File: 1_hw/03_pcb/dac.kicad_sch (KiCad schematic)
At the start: 6 parts, among them U17 AD9850, U18 AD9744

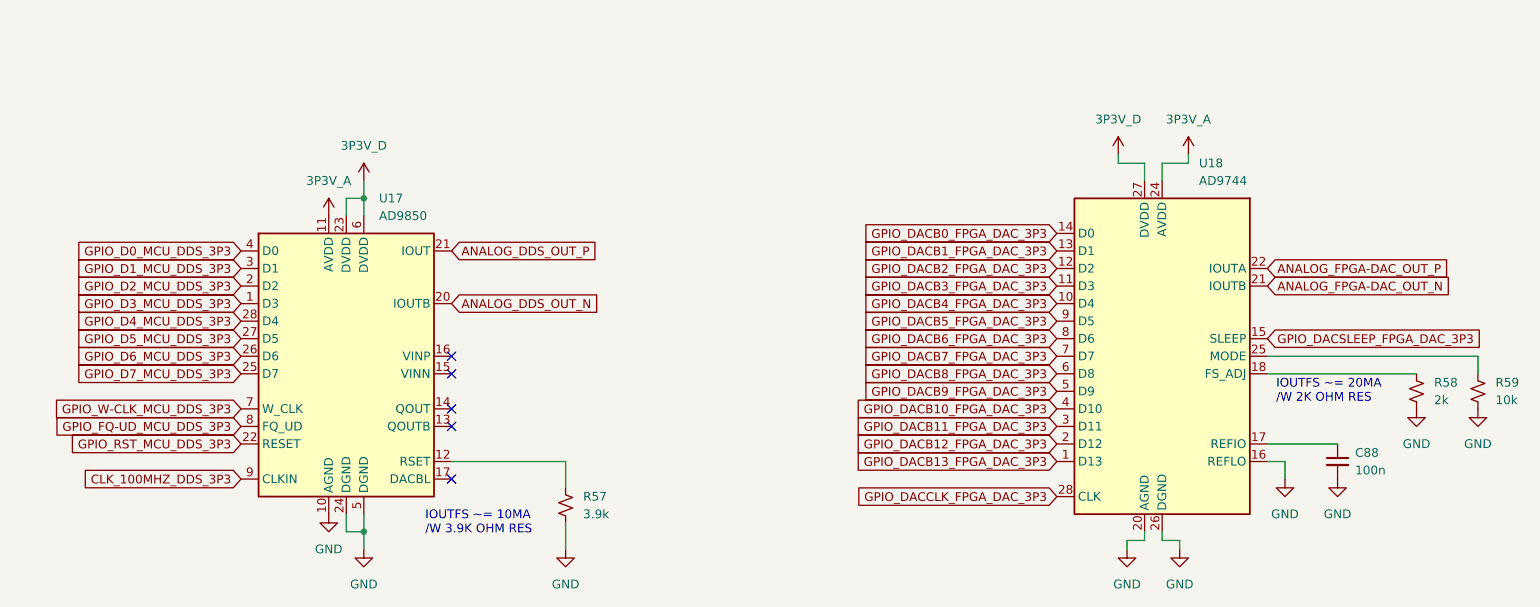
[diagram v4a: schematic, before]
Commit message: FEAT: Initial board placement started.
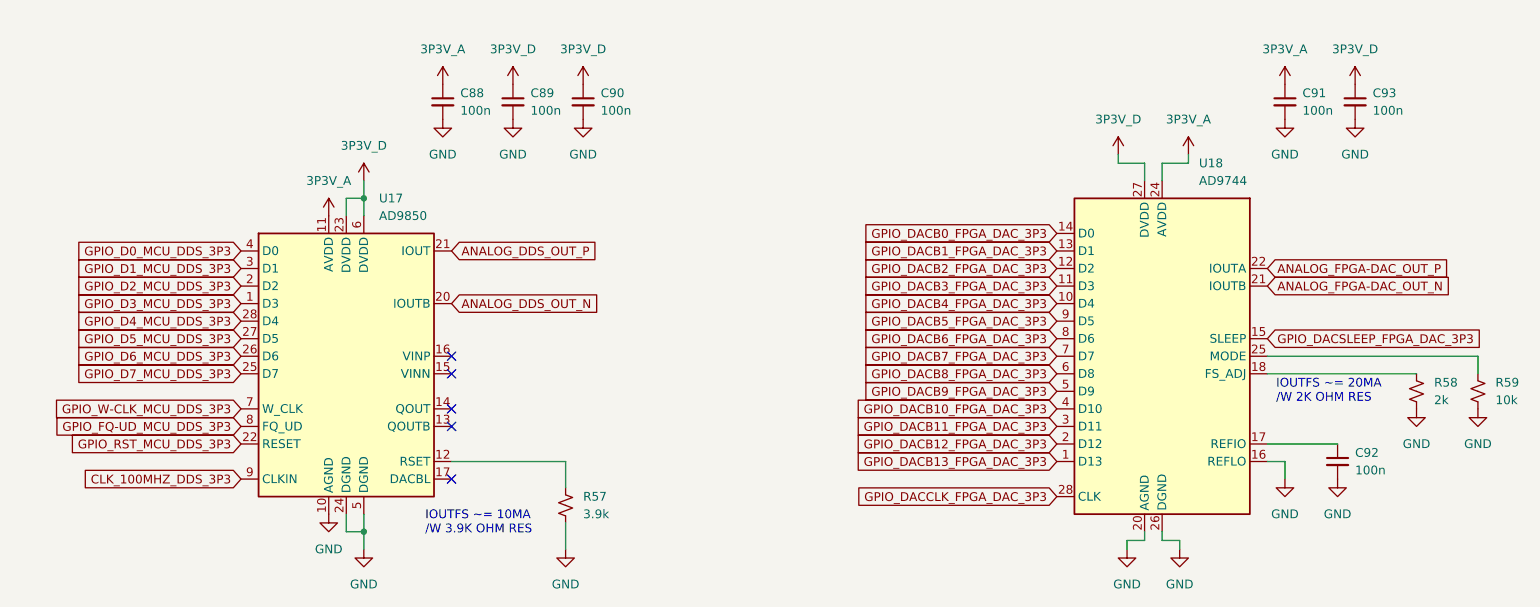
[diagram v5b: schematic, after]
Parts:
- added C88, C89, C90, C91, C93: 100n, Capacitor_SMD:C_0603_1608Metric, symbol Device:C_Small
- renumbered C88 to C92
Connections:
- net 3P3V_A: now also C88.1, C91.1
- net 3P3V_D: now also C89.1, C90.1, C93.1
- net GND: now also C88.2, C89.2, C90.2, C91.2, C93.2
- new net: U18.19 (NC), U18.23 (NC)

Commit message: FEAT: Changed Inductor to higher current. Continued layout. Assigned some Netclasses.
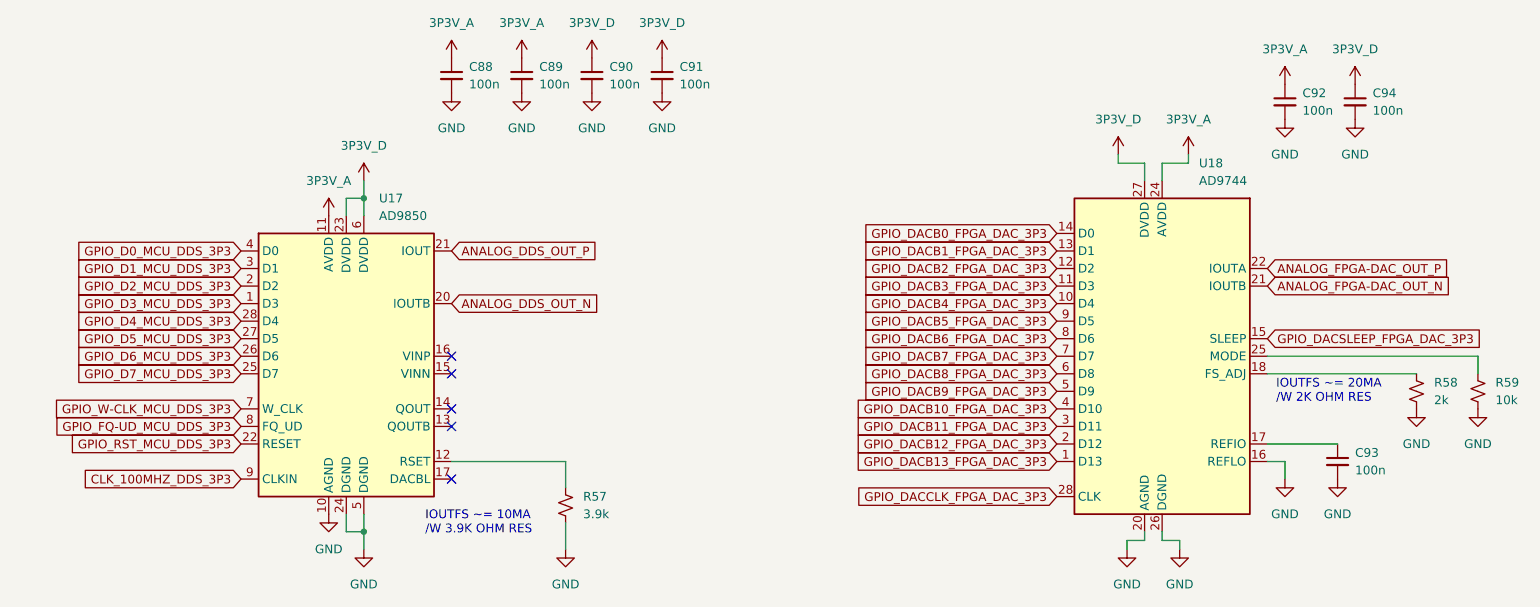
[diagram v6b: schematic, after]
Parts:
- added C88: 100n, Capacitor_SMD:C_0603_1608Metric, symbol Device:C_Small
- renumbered C88 to C89, C89 to C90, C90 to C91, C91 to C92, C92 to C93, C93 to C94
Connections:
- net 3P3V_A: now also C88.1
- net GND: now also C88.2
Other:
- moved on the sheet: C89, C90, C91
